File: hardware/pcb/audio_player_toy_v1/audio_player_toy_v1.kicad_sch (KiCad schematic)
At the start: 13 parts, among them J1 Conn_02x05_Odd_Even, U1 BH-AAA-B5AA005, U2 ISD2360YYI

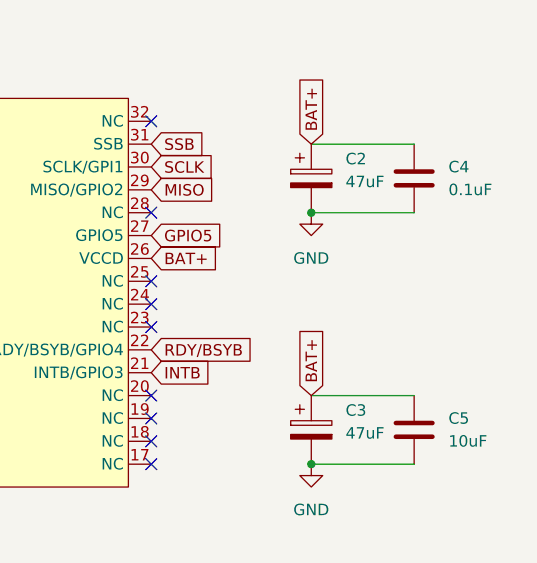
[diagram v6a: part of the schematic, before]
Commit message: chore: update decoupling caps in v1
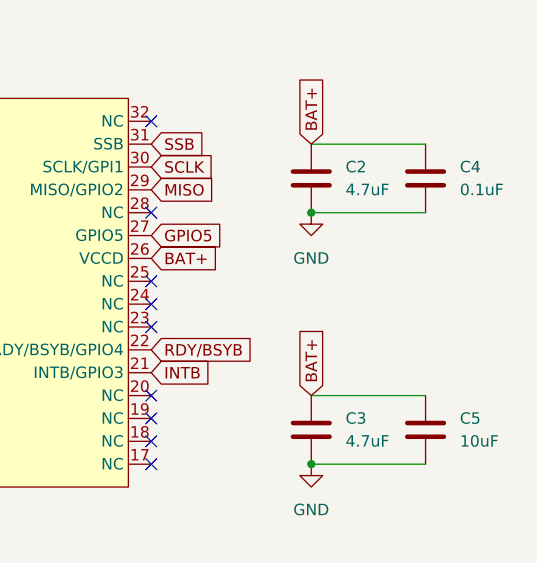
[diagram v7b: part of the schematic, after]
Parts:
- removed C2, C3: 47uF, .pretty:CASE-A_3216, symbol Device:C_Polarized
- added C2, C3: 4.7uF, Capacitor_SMD:C_0603_1608Metric, symbol Device:C
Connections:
- net BAT+: now also C2.1, C3.1
- net GND: now also C2.2, C3.2
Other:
- moved on the sheet: C4, C5
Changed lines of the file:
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@@
 	(paper "A4")
+	(junction
+		(at 22.86 64.77)
+		(diameter 0)
+		(color 0 0 0 0)
+	)
+	(junction
+		(at 107.95 54.61)
+		(diameter 0)
+		(color 0 0 0 0)
+	)
+	(junction
+		(at 78.74 22.86)
+		(diameter 0)
+		(color 0 0 0 0)
+	)
+	(junction
+		(at 176.53 64.77)
+		(diameter 0)
+		(color 0 0 0 0)
+	)
 	(junction
 		(at 176.53 36.83)
@@
 	)
 	(junction
-		(at 22.86 64.77)
-		(diameter 0)
-		(color 0 0 0 0)
-	)
-	(junction
-		(at 107.95 54.61)
-		(diameter 0)
-		(color 0 0 0 0)
-	)
-	(junction
-		(at 78.74 22.86)
-		(diameter 0)
-		(color 0 0 0 0)
-	)
-	(junction
 		(at 63.5 60.96)
 		(diameter 0)
 		(color 0 0 0 0)
 	)
-	(junction
-		(at 176.53 64.77)
-		(diameter 0)
-		(color 0 0 0 0)
-	)
 	(no_connect
 		(at 107.95 29.21)
@@
 	(wire
 		(pts
-			(xy 176.53 57.15) (xy 187.96 57.15)
+			(xy 176.53 57.15) (xy 189.23 57.15)
 		)
 		(stroke
@@
 	(wire
 		(pts
-			(xy 176.53 36.83) (xy 187.96 36.83)
+			(xy 176.53 36.83) (xy 189.23 36.83)
 		)
 		(stroke
@@
 	(wire
 		(pts
-			(xy 176.53 64.77) (xy 187.96 64.77)
+			(xy 176.53 64.77) (xy 189.23 64.77)
 		)
 		(stroke
@@
 	(wire
 		(pts
-			(xy 176.53 29.21) (xy 187.96 29.21)
+			(xy 176.53 29.21) (xy 189.23 29.21)
 		)
 		(stroke
@@
 	(symbol
 		(lib_id "Device:C")
-		(at 187.96 60.96 0)
+		(at 189.23 60.96 0)
 		(unit 1)
 		(exclude_from_sim no)
@@
 		(fields_autoplaced yes)
 		(property "Reference" "C5"
-			(at 191.77 59.6899 0)
+			(at 193.04 59.6899 0)
 			(effects
 				(font
@@
 		)
 		(property "Value" "10uF"
-			(at 191.77 62.2299 0)
+			(at 193.04 62.2299 0)
 			(effects
 				(font
@@
 		)
 		(property "Footprint" "Resistor_SMD:R_0603_1608Metric"
-			(at 188.9252 64.77 0)
+			(at 190.1952 64.77 0)
 			(effects
 				(font
@@
 		)
 		(property "Datasheet" "~"
-			(at 187.96 60.96 0)
+			(at 189.23 60.96 0)
 			(effects
 				(font
@@
 		)
 		(property "Description" "Unpolarized capacitor"
-			(at 187.96 60.96 0)
+			(at 189.23 60.96 0)
 			(effects
 				(font
@@
 		)
 		(property "Manufactor" ""
-			(at 187.96 60.96 0)
+			(at 189.23 60.96 0)
 			(effects
 				(font
@@
 	(symbol
 		(lib_id "Device:C")
-		(at 187.96 33.02 0)
+		(at 189.23 33.02 0)
 		(unit 1)
 		(exclude_from_sim no)
@@
 		(fields_autoplaced yes)
 		(property "Reference" "C4"
-			(at 191.77 31.7499 0)
+			(at 193.04 31.7499 0)
 			(effects
 				(font
@@
 		)
 		(property "Value" "0.1uF"
-			(at 191.77 34.2899 0)
+			(at 193.04 34.2899 0)
 			(effects
 				(font
@@
 		)
 		(property "Footprint" "Resistor_SMD:R_0603_1608Metric"
-			(at 188.9252 36.83 0)
+			(at 190.1952 36.83 0)
 			(effects
 				(font
@@
 		)
 		(property "Datasheet" "~"
-			(at 187.96 33.02 0)
+			(at 189.23 33.02 0)
 			(effects
 				(font
@@
 		)
 		(property "Description" "Unpolarized capacitor"
-			(at 187.96 33.02 0)
+			(at 189.23 33.02 0)
 			(effects
 				(font
@@
 		)
 		(property "Manufactor" ""
-			(at 187.96 33.02 0)
+			(at 189.23 33.02 0)
 			(effects
 				(font
@@
 	)
 	(symbol
-		(lib_id "Device:C_Polarized")
+		(lib_id "Device:C")
 		(at 176.53 60.96 0)
 		(unit 1)
@@
 		(fields_autoplaced yes)
 		(property "Reference" "C3"
-			(at 180.34 58.8009 0)
-			(effects
-				(font
-					(size 1.27 1.27)
-				)
-				(justify left)
-			)
-		)
-		(property "Value" "47uF"
-			(at 180.34 61.3409 0)
-			(effects
-				(font
-					(size 1.27 1.27)
-				)
-				(justify left)
-			)
-		)
-		(property "Footprint" ".pretty:CASE-A_3216"
+			(at 180.34 59.6899 0)
+			(effects
+				(font
+					(size 1.27 1.27)
+				)
+				(justify left)
+			)
+		)
+		(property "Value" "4.7uF"
+			(at 180.34 62.2299 0)
+			(effects
+				(font
+					(size 1.27 1.27)
+				)
+				(justify left)
+			)
+		)
+		(property "Footprint" "Capacitor_SMD:C_0603_1608Metric"
 			(at 177.4952 64.77 0)
 			(effects
@@
 			)
 		)
-		(property "Description" "Polarized capacitor"
+		(property "Description" "Unpolarized capacitor"
 			(at 176.53 60.96 0)
 			(effects
@@
 			)
 		)
-		(property "Component" "TLJA476M010R0600"
-			(at 176.53 60.96 0)
-			(effects
-				(font
-					(size 1.27 1.27)
-				)
-				(hide yes)
-			)
-		)
-		(property "Detail" "+-20%, 10V, 600mΩ"
-			(at 176.53 60.96 0)
-			(effects
-				(font
-					(size 1.27 1.27)
-				)
-				(hide yes)
-			)
-		)
-		(property "Manufactor" "KYOCERA AVX"
-			(at 176.53 60.96 0)
-			(effects
-				(font
-					(size 1.27 1.27)
-				)
-				(hide yes)
-			)
+		(pin "1"
 		)
 		(pin "2"
-		)
-		(pin "1"
 		)
 		(instances
@@
 	)
 	(symbol
-		(lib_id "Device:C_Polarized")
+		(lib_id "Device:C")
 		(at 176.53 33.02 0)
 		(unit 1)
@@
 		(fields_autoplaced yes)
 		(property "Reference" "C2"
-			(at 180.34 30.8609 0)
-			(effects
-				(font
-					(size 1.27 1.27)
-				)
-				(justify left)
-			)
-		)
-		(property "Value" "47uF"
-			(at 180.34 33.4009 0)
-			(effects
-				(font
-					(size 1.27 1.27)
-				)
-				(justify left)
-			)
-		)
-		(property "Footprint" ".pretty:CASE-A_3216"
+			(at 180.34 31.7499 0)
+			(effects
+				(font
+					(size 1.27 1.27)
+				)
+				(justify left)
+			)
+		)
+		(property "Value" "4.7uF"
+			(at 180.34 34.2899 0)
+			(effects
+				(font
+					(size 1.27 1.27)
+				)
+				(justify left)
+			)
+		)
+		(property "Footprint" "Capacitor_SMD:C_0603_1608Metric"
 			(at 177.4952 36.83 0)
 			(effects
@@
 			)
 		)
-		(property "Description" "Polarized capacitor"
+		(property "Description" "Unpolarized capacitor"
 			(at 176.53 33.02 0)
 			(effects
@@
 			)
 		)
-		(property "Component" "TLJA476M010R0600"
-			(at 176.53 33.02 0)
-			(effects
-				(font
-					(size 1.27 1.27)
-				)
-				(hide yes)
-			)
-		)
-		(property "Detail" "+-20%, 10V, 600mΩ"
-			(at 176.53 33.02 0)
-			(effects
-				(font
-					(size 1.27 1.27)
-				)
-				(hide yes)
-			)
-		)
-		(property "Manufactor" "KYOCERA AVX"
-			(at 176.53 33.02 0)
-			(effects
-				(font
-					(size 1.27 1.27)
-				)
-				(hide yes)
-			)
+		(pin "1"
 		)
 		(pin "2"
 		)
-		(pin "1"
-		)
 		(instances

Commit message: fix: fix annotation
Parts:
- C2, C3: Component (none) -> GRM188Z71C475KE21D; Detail (none) -> +-10%, 16V, X7R; Manufactor (none) -> MuRata
- C4: Component (none) -> GCJ188R71C104KA01D; Detail (none) -> +-10%, 16V, X7R; Manufactor (none) -> MuRata
- C5: Component (none) -> GRM188R61C106KAALD; Detail (none) -> +-10%, 16V, X5R; Manufactor (none) -> MuRata
- renumbered R3 to R1, S3 to S1
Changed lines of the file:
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@@
 			)
 		)
-		(property "Manufactor" ""
+		(property "Manufactor" "MuRata"
+			(at 189.23 60.96 0)
+			(effects
+				(font
+					(size 1.27 1.27)
+				)
+				(hide yes)
+			)
+		)
+		(property "Component" "GRM188R61C106KAALD"
+			(at 189.23 60.96 0)
+			(effects
+				(font
+					(size 1.27 1.27)
+				)
+				(hide yes)
+			)
+		)
+		(property "Detail" "+-10%, 16V, X5R"
 			(at 189.23 60.96 0)
 			(effects
@@
 			)
 		)
-		(property "Manufactor" ""
+		(property "Manufactor" "MuRata"
+			(at 189.23 33.02 0)
+			(effects
+				(font
+					(size 1.27 1.27)
+				)
+				(hide yes)
+			)
+		)
+		(property "Component" "GCJ188R71C104KA01D"
+			(at 189.23 33.02 0)
+			(effects
+				(font
+					(size 1.27 1.27)
+				)
+				(hide yes)
+			)
+		)
+		(property "Detail" "+-10%, 16V, X7R"
 			(at 189.23 33.02 0)
 			(effects
@@
 		(dnp no)
 		(fields_autoplaced yes)
-		(property "Reference" "S3"
+		(property "Reference" "S1"
 			(at 72.39 52.07 0)
 			(effects
@@
 			(project "audio_player_toy_v1"
 				(path "/cc88cd3f-6086-49ef-b4e9-3dfe485946b1"
-					(reference "S3")
+					(reference "S1")
 					(unit 1)
 				)
@@
 			)
 		)
+		(property "Component" "GRM188Z71C475KE21D"
+			(at 176.53 60.96 0)
+			(effects
+				(font
+					(size 1.27 1.27)
+				)
+				(hide yes)
+			)
+		)
+		(property "Detail" "+-10%, 16V, X7R"
+			(at 176.53 60.96 0)
+			(effects
+				(font
+					(size 1.27 1.27)
+				)
+				(hide yes)
+			)
+		)
+		(property "Manufactor" "MuRata"
+			(at 176.53 60.96 0)
+			(effects
+				(font
+					(size 1.27 1.27)
+				)
+				(hide yes)
+			)
+		)
 		(pin "1"
 		)
@@
 		(dnp no)
 		(fields_autoplaced yes)
-		(property "Reference" "#PWR011"
+		(property "Reference" "#PWR09"
 			(at 176.53 71.12 0)
 			(effects
@@
 			(project "audio_player_toy_v1"
 				(path "/cc88cd3f-6086-49ef-b4e9-3dfe485946b1"
-					(reference "#PWR011")
+					(reference "#PWR09")
 					(unit 1)
 				)
@@
 		(dnp no)
 		(fields_autoplaced yes)
-		(property "Reference" "#PWR09"
+		(property "Reference" "#PWR07"
 			(at 133.35 15.24 0)
 			(effects
@@
 			(project ""
 				(path "/cc88cd3f-6086-49ef-b4e9-3dfe485946b1"
-					(reference "#PWR09")
+					(reference "#PWR07")
 					(unit 1)
 				)
@@
 		(dnp no)
 		(fields_autoplaced yes)
-		(property "Reference" "#PWR08"
+		(property "Reference" "#PWR06"
 			(at 101.6 54.61 0)
 			(effects
@@
 			(project "audio_player_toy_v1"
 				(path "/cc88cd3f-6086-49ef-b4e9-3dfe485946b1"
-					(reference "#PWR08")
+					(reference "#PWR06")
 					(unit 1)
 				)
@@
 		(on_board yes)
 		(dnp no)
-		(property "Reference" "R3"
+		(property "Reference" "R1"
 			(at 59.69 54.356 0)
 			(effects
@@
 			(project "audio_player_toy_v1"
 				(path "/cc88cd3f-6086-49ef-b4e9-3dfe485946b1"
-					(reference "R3")
+					(reference "R1")
 					(unit 1)
 				)
@@
 		(dnp no)
 		(fields_autoplaced yes)
-		(property "Reference" "#PWR06"
+		(property "Reference" "#PWR04"
 			(at 80.01 67.31 0)
 			(effects
@@
 			(project "audio_player_toy_v1"
 				(path "/cc88cd3f-6086-49ef-b4e9-3dfe485946b1"
-					(reference "#PWR06")
+					(reference "#PWR04")
 					(unit 1)
 				)
@@
 		(dnp no)
 		(fields_autoplaced yes)
-		(property "Reference" "#PWR07"
+		(property "Reference" "#PWR05"
 			(at 101.6 34.29 0)
 			(effects
@@
 			(project "audio_player_toy_v1"
 				(path "/cc88cd3f-6086-49ef-b4e9-3dfe485946b1"
-					(reference "#PWR07")
+					(reference "#PWR05")
 					(unit 1)
 				)
@@
 			)
 		)
+		(property "Component" "GRM188Z71C475KE21D"
+			(at 176.53 33.02 0)
+			(effects
+				(font
+					(size 1.27 1.27)
+				)
+				(hide yes)
+			)
+		)
+		(property "Detail" "+-10%, 16V, X7R"
+			(at 176.53 33.02 0)
+			(effects
+				(font
+					(size 1.27 1.27)
+				)
+				(hide yes)
+			)
+		)
+		(property "Manufactor" "MuRata"
+			(at 176.53 33.02 0)
+			(effects
+				(font
+					(size 1.27 1.27)
+				)
+				(hide yes)
+			)
+		)
 		(pin "1"
 		)
@@
 		(dnp no)
 		(fields_autoplaced yes)
-		(property "Reference" "#PWR010"
+		(property "Reference" "#PWR08"
 			(at 176.53 43.18 0)
 			(effects
@@
 			(project "audio_player_toy_v1"
 				(path "/cc88cd3f-6086-49ef-b4e9-3dfe485946b1"
-					(reference "#PWR010")
-					(unit 1)
-				)
+					(reference "#PWR08")
+					(unit 1)
+				)
